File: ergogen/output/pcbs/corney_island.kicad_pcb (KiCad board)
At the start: 2 copper layers, 133.8 x 91.7 mm, 101 parts

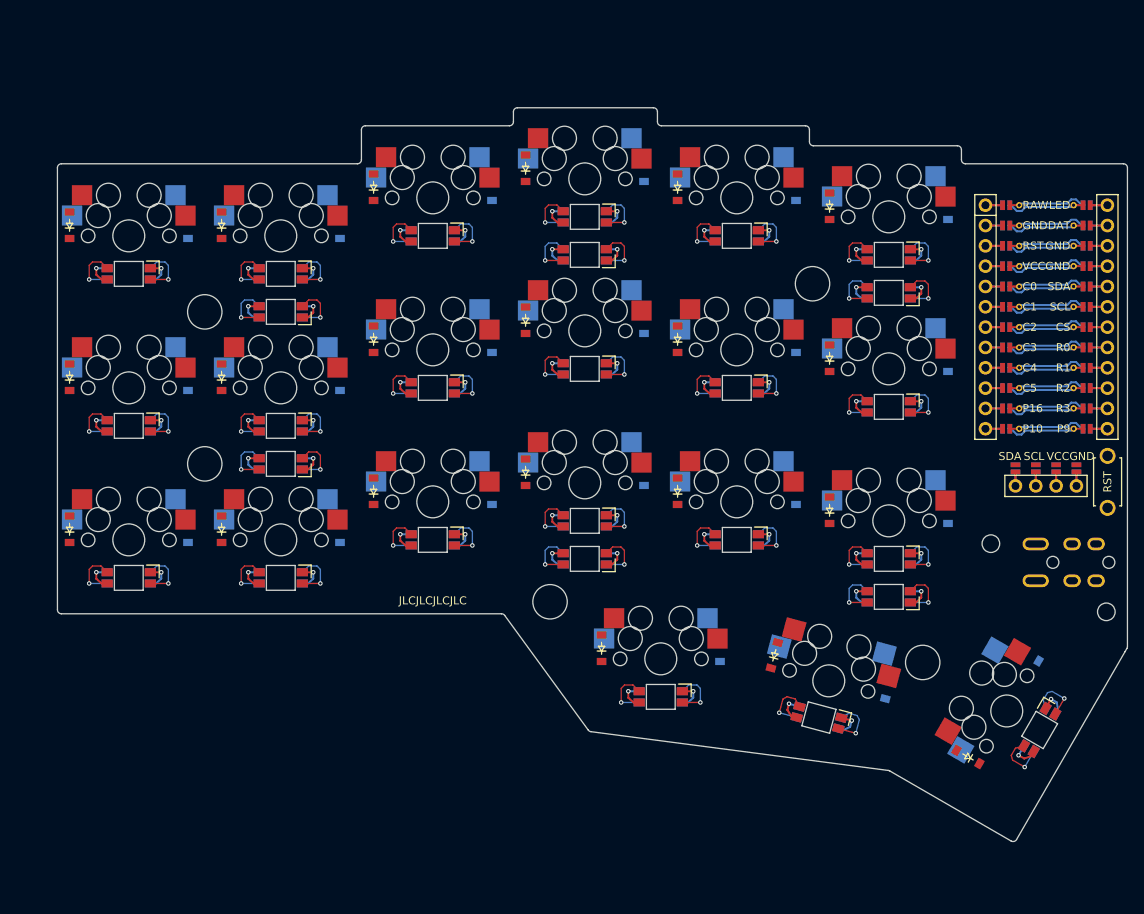
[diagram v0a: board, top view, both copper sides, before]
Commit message: Removed outer column
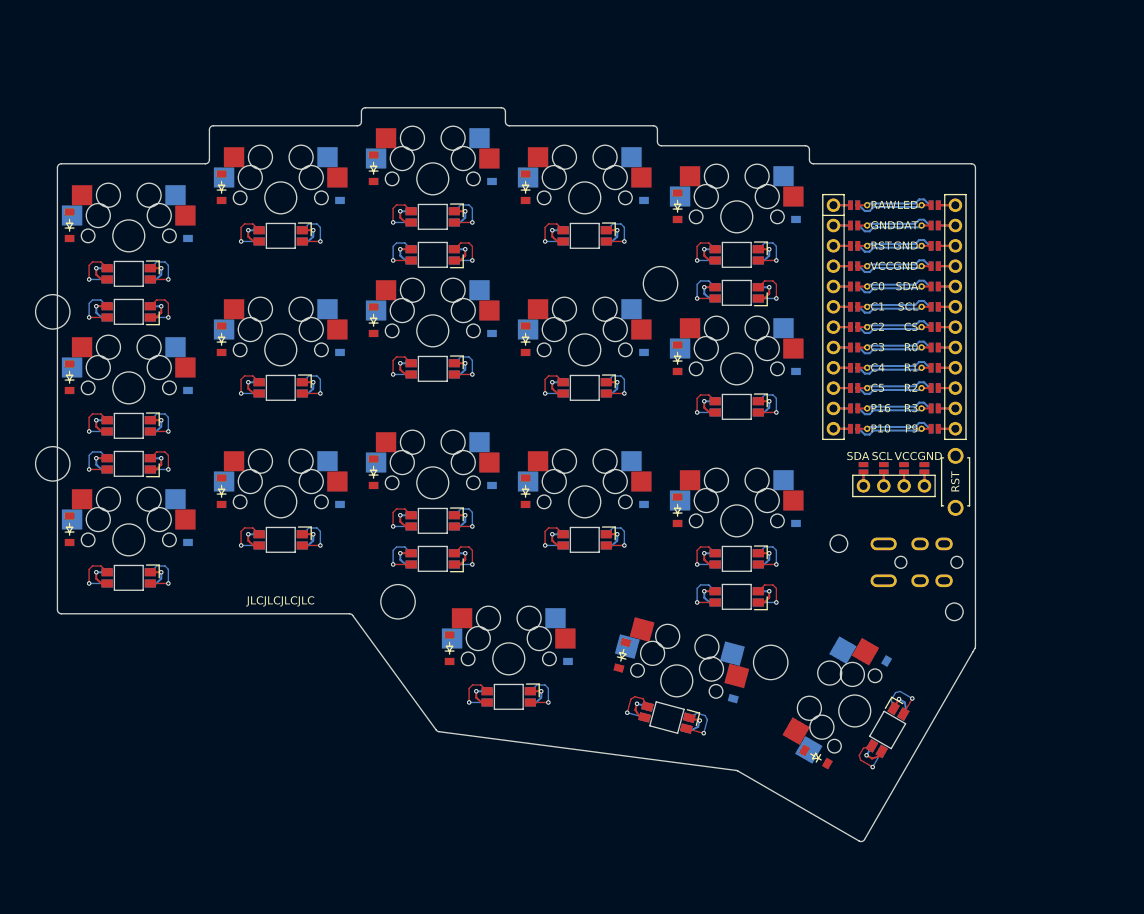
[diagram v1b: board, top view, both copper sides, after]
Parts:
- removed D37, D38, D39, D40, D41, D42: , ceoloide:diode_tht_sod123
- removed LED25, LED26, LED27: , ceoloide:led_SK6812mini-e (underglow, reversible)
- removed S19, S20, S21: , MX
- D19, D20, D21: moved to F.Cu
- LED19, LED20, LED21: footprint ceoloide:led_SK6812mini-e (per-key, reversible) -> ceoloide:led_SK6812mini-e (underglow, reversible)
- moved D21 131.2 mm to (92.6, 60.7), turned to 90 degrees
- moved LED21 125.3 mm to (100.0, 71.5), turned to 180 degrees
- moved D20 109.4 mm to (92.6, 79.7), turned to 90 degrees
- moved LED22 97.4 mm to (100.0, 90.5)
- moved D19 82.6 mm to (92.6, 98.7)
- moved LED20 75.3 mm to (138.0, 64.4), turned to 180 degrees
- moved D36 73.3 mm to (185.9, 127.1), turned to 150 degrees
- moved LED24 67.2 mm to (176.0, 107.1)
- moved S18 61.9 mm to (190.7, 121.4), turned to 60 degrees
- moved LED18 59.4 mm to (194.9, 123.8), turned to 240 degrees
- moved D18 56.8 mm to (193.3, 114.3), turned to 150 degrees
- moved LED19 51.4 mm to (176.0, 69.1)
- moved D16 50.5 mm to (154.9, 113.5)
- moved LED16 50.5 mm to (147.5, 119.6)
- moved S16 50.5 mm to (147.5, 114.9)
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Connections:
- D1 pad 2: outer_bottom -> pinky_bottom
- D10 pad 2: middle_bottom -> index_bottom
- D11 pad 2: middle_home -> index_home
- D12 pad 2: middle_top -> index_top
- D13 pad 2: index_bottom -> inner_bottom
- D14 pad 2: index_home -> inner_home
- D15 pad 2: index_top -> inner_top
- D16 pad 1: R2 -> R3
- D16 pad 2: inner_bottom -> near_home
- D17 pad 1: R1 -> R3
- D17 pad 2: inner_home -> mid_home
- D18 pad 1: R0 -> R3
- D18 pad 2: inner_top -> far_home
- D19 pad 1: R3 -> R2
- D19 pad 2: near_home -> pinky_bottom
- D2 pad 2: outer_home -> pinky_home
- D20 pad 1: R3 -> R1
- D20 pad 2: mid_home -> pinky_home
- D21 pad 1: R3 -> R0
- D21 pad 2: far_home -> pinky_top
- D22 pad 2: outer_bottom -> ring_bottom
- D23 pad 2: outer_home -> ring_home
- D24 pad 2: outer_top -> ring_top
- D25 pad 2: pinky_bottom -> middle_bottom
- D26 pad 2: pinky_home -> middle_home
- D27 pad 2: pinky_top -> middle_top
- D28 pad 2: ring_bottom -> index_bottom
- D29 pad 2: ring_home -> index_home
- D3 pad 2: outer_top -> pinky_top
- D30 pad 2: ring_top -> index_top
- D31 pad 2: middle_bottom -> inner_bottom
- D32 pad 2: middle_home -> inner_home
- D33 pad 2: middle_top -> inner_top
- D34 pad 1: R2 -> R3
- D34 pad 2: index_bottom -> near_home
- D35 pad 1: R1 -> R3
- D35 pad 2: index_home -> mid_home
- D36 pad 1: R0 -> R3
- D36 pad 2: index_top -> far_home
- D4 pad 2: pinky_bottom -> ring_bottom
- D5 pad 2: pinky_home -> ring_home
- D6 pad 2: pinky_top -> ring_top
- D7 pad 2: ring_bottom -> middle_bottom
- D8 pad 2: ring_home -> middle_home
- D9 pad 2: ring_top -> middle_top
- LED1 pad 2: LED_21 -> LED_16
- LED1 pad 4: LED_20 -> LED_15
- LED10 pad 2: LED_10 -> LED_7
- LED10 pad 4: LED_9 -> LED_6
- LED11 pad 2: LED_11 -> LED_6
- LED11 pad 4: LED_10 -> LED_5
- LED12 pad 2: LED_12 -> LED_5
- LED12 pad 4: LED_11 -> LED_4
- LED13 pad 2: LED_7 -> LED_2
- LED13 pad 4: LED_6 -> LED_1
- LED14 pad 2: LED_6 -> LED_3
- LED14 pad 4: LED_5 -> LED_2
- LED15 pad 2: LED_5 -> LED_4
- LED15 pad 4: LED_4 -> LED_3
- LED16 pad 2: LED_2 -> LED_9
- LED16 pad 4: LED_1 -> LED_8
- LED17 pad 2: LED_3 -> LED_8
- LED17 pad 4: LED_2 -> LED_7
- LED18 pad 2: LED_4 -> LED_1
- LED18 pad 4: LED_3 -> ULED_6
- LED19 pad 2: LED_9 -> ULED_1
- LED19 pad 4: LED_8 -> LED
- LED2 pad 2: LED_20 -> LED_17
- LED2 pad 4: LED_19 -> LED_16
- LED20 pad 2: LED_8 -> ULED_2
- LED20 pad 4: LED_7 -> ULED_1
- LED21 pad 2: LED_1 -> ULED_3
- LED21 pad 4: ULED_6 -> ULED_2
- LED22 pad 2: ULED_1 -> ULED_4
- LED22 pad 4: LED -> ULED_3
- LED23 pad 2: ULED_2 -> ULED_5
- LED23 pad 4: ULED_1 -> ULED_4
- LED24 pad 2: ULED_3 -> ULED_6
- LED24 pad 4: ULED_2 -> ULED_5
- LED3 pad 2: LED_19 -> LED_18
- LED3 pad 4: LED_18 -> LED_17
- LED4 pad 2: LED_16 -> LED_15
- LED4 pad 4: LED_15 -> LED_14
- LED5 pad 2: LED_17 -> LED_14
- LED5 pad 4: LED_16 -> LED_13
- LED6 pad 2: LED_18 -> LED_13
- LED6 pad 4: LED_17 -> LED_12
- LED7 pad 2: LED_15 -> LED_10
- LED7 pad 4: LED_14 -> LED_9
- LED8 pad 2: LED_14 -> LED_11
- LED8 pad 4: LED_13 -> LED_10
- LED9 pad 2: LED_13 -> LED_12
- LED9 pad 4: LED_12 -> LED_11
- MCU1 pad 1: MCU1_1 -> LED
- MCU1 pad 10: MCU1_10 -> R2
- MCU1 pad 11: MCU1_11 -> R3
- MCU1 pad 12: MCU1_12 -> P9
- MCU1 pad 2: MCU1_2 -> DAT
- MCU1 pad 3: MCU1_3 -> GND
- MCU1 pad 4: MCU1_4 -> GND
- MCU1 pad 5: MCU1_5 -> SDA
- MCU1 pad 6: MCU1_6 -> SCL
- MCU1 pad 7: MCU1_7 -> CS
- MCU1 pad 8: MCU1_8 -> R0
- MCU1 pad 9: MCU1_9 -> R1
- S1 pad 1: C0 -> C1
- S1 pad 2: outer_bottom -> pinky_bottom
- S10 pad 1: C3 -> C4
- S10 pad 2: middle_bottom -> index_bottom
- S11 pad 1: C3 -> C4
- S11 pad 2: middle_home -> index_home
- S12 pad 1: C3 -> C4
- S12 pad 2: middle_top -> index_top
- S13 pad 1: C4 -> C5
- S13 pad 2: index_bottom -> inner_bottom
- S14 pad 1: C4 -> C5
- S14 pad 2: index_home -> inner_home
- S15 pad 1: C4 -> C5
- S15 pad 2: index_top -> inner_top
- S16 pad 1: C5 -> C3
- S16 pad 2: inner_bottom -> near_home
- S17 pad 1: C5 -> C4
- S17 pad 2: inner_home -> mid_home
- S18 pad 2: inner_top -> far_home
- S2 pad 1: C0 -> C1
- S2 pad 2: outer_home -> pinky_home
- S3 pad 1: C0 -> C1
- S3 pad 2: outer_top -> pinky_top
- S4 pad 1: C1 -> C2
- S4 pad 2: pinky_bottom -> ring_bottom
- S5 pad 1: C1 -> C2
- S5 pad 2: pinky_home -> ring_home
- S6 pad 1: C1 -> C2
- S6 pad 2: pinky_top -> ring_top
- S7 pad 1: C2 -> C3
- S7 pad 2: ring_bottom -> middle_bottom
- S8 pad 1: C2 -> C3
- S8 pad 2: ring_home -> middle_home
- S9 pad 1: C2 -> C3
- S9 pad 2: ring_top -> middle_top
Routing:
- net inner_top: track 0.00 -> 101.6 mm
- net pinky_bottom: track 0.00 -> 101.4 mm
- net far_home: track 0.00 -> 50.9 mm
- net R2: track 9.63 -> 50.9 mm
- net GND: track 130.3 -> 93.6 mm, vias 27 -> 24
- net VCC: track 111.0 -> 93.6 mm, vias 27 -> 24
- net LED_20: track 13.5 -> 0.00 mm, vias 2 -> 0
- net LED_19: track 13.5 -> 0.00 mm, vias 2 -> 0
- net C3: track 9.64 -> 0.00 mm
- net RST: track 9.64 -> 0.00 mm
- net RAW: track 9.64 -> 0.00 mm
- net P16: track 9.64 -> 0.00 mm
- net C2: track 9.64 -> 0.00 mm
- net C0: track 9.64 -> 0.00 mm
- net P10: track 9.64 -> 0.00 mm
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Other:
- board size 133.8 x 91.7 mm -> 114.8 x 91.7 mm

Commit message: Changed stagger to be like karia
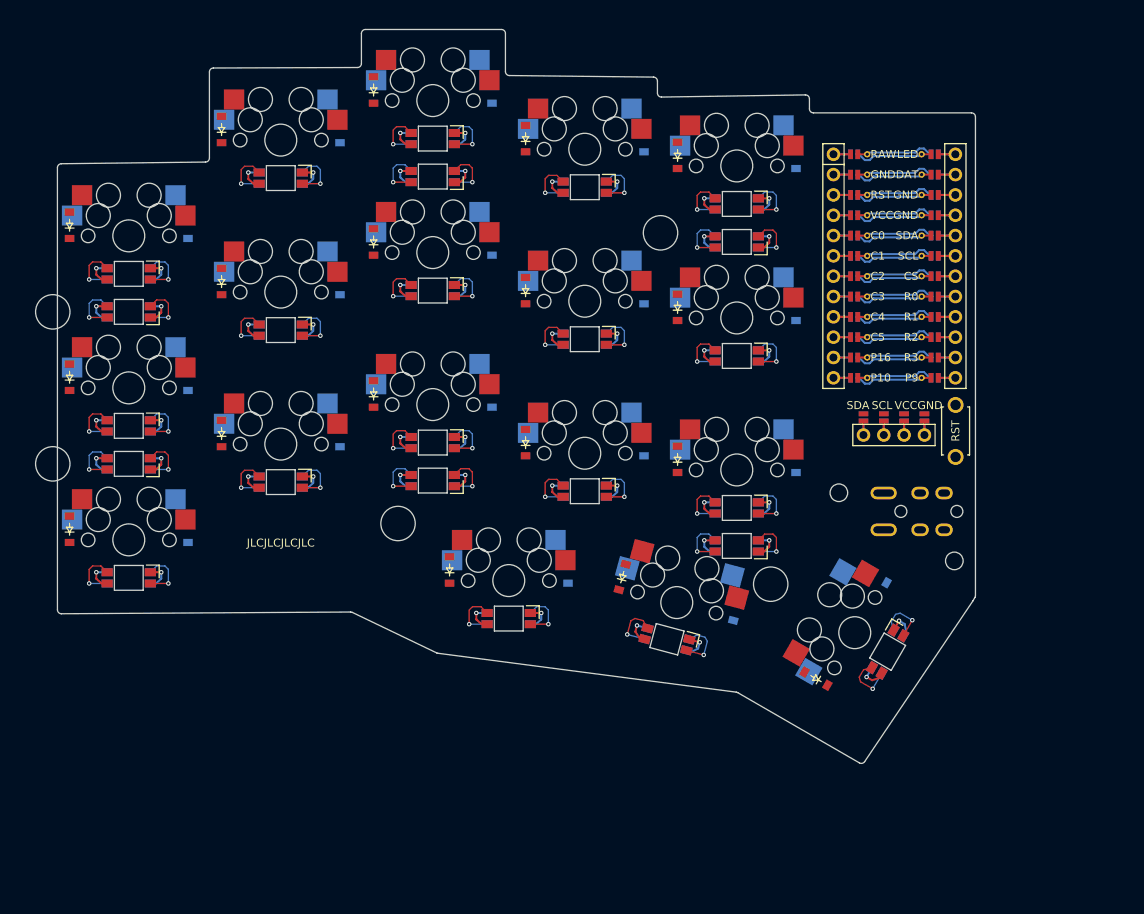
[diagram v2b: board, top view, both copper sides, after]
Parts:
- moved D16 9.78 mm to (154.9, 103.8)
- moved D17 9.78 mm to (176.0, 108.5)
- moved D18 9.78 mm to (193.3, 104.5)
- moved D25 9.78 mm to (130.6, 81.8)
- moved D26 9.78 mm to (130.6, 62.8)
- moved D27 9.78 mm to (130.6, 43.8)
- moved D34 9.78 mm to (140.1, 103.8)
- moved D35 9.78 mm to (161.7, 104.6)
- moved D36 9.78 mm to (185.9, 117.4)
- moved D7 9.78 mm to (145.4, 81.8)
- moved D8 9.78 mm to (145.4, 62.8)
- moved D9 9.78 mm to (145.4, 43.8)
- moved LED16 9.78 mm to (147.5, 109.8)
- moved LED17 9.78 mm to (167.3, 112.4)
- moved LED18 9.78 mm to (194.9, 114.0)
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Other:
- outline, holes or cut-outs redrawn

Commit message: Added splay to pinky
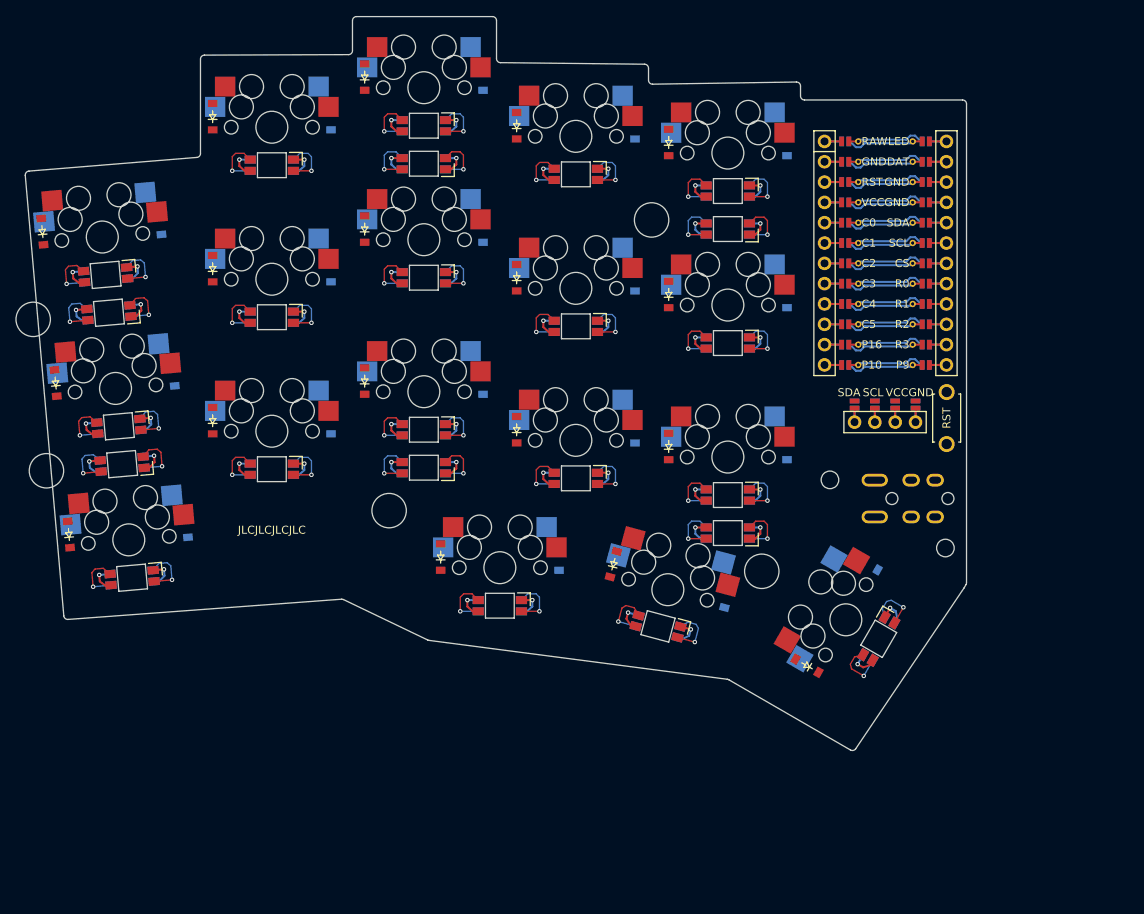
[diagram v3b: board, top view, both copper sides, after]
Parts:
- moved D3 3.49 mm to (103.9, 60.2), turned to 95 degrees
- moved D21 3.49 mm to (89.2, 61.5), turned to 95 degrees
- moved S3 3.32 mm to (96.7, 62.1), turned to 5 degrees
- moved LED3 2.90 mm to (97.1, 66.9), turned to 185 degrees
- moved MH3 2.62 mm to (88.1, 72.4), turned to 5 degrees
- moved LED21 2.49 mm to (97.5, 71.6), turned to 185 degrees
- moved LED17 1.96 mm to (166.2, 110.8)
- moved D16 1.96 mm to (153.8, 102.2)
- moved D17 1.96 mm to (174.9, 106.9)
- moved D18 1.96 mm to (192.2, 102.9)
- moved D25 1.96 mm to (129.5, 80.2)
- moved D26 1.96 mm to (129.5, 61.2)
- moved D27 1.96 mm to (129.5, 42.2)
- moved D34 1.96 mm to (139.0, 102.2)
- moved D35 1.96 mm to (160.6, 103.0)
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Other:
- board size 114.8 x 91.7 mm -> 117.7 x 91.7 mm

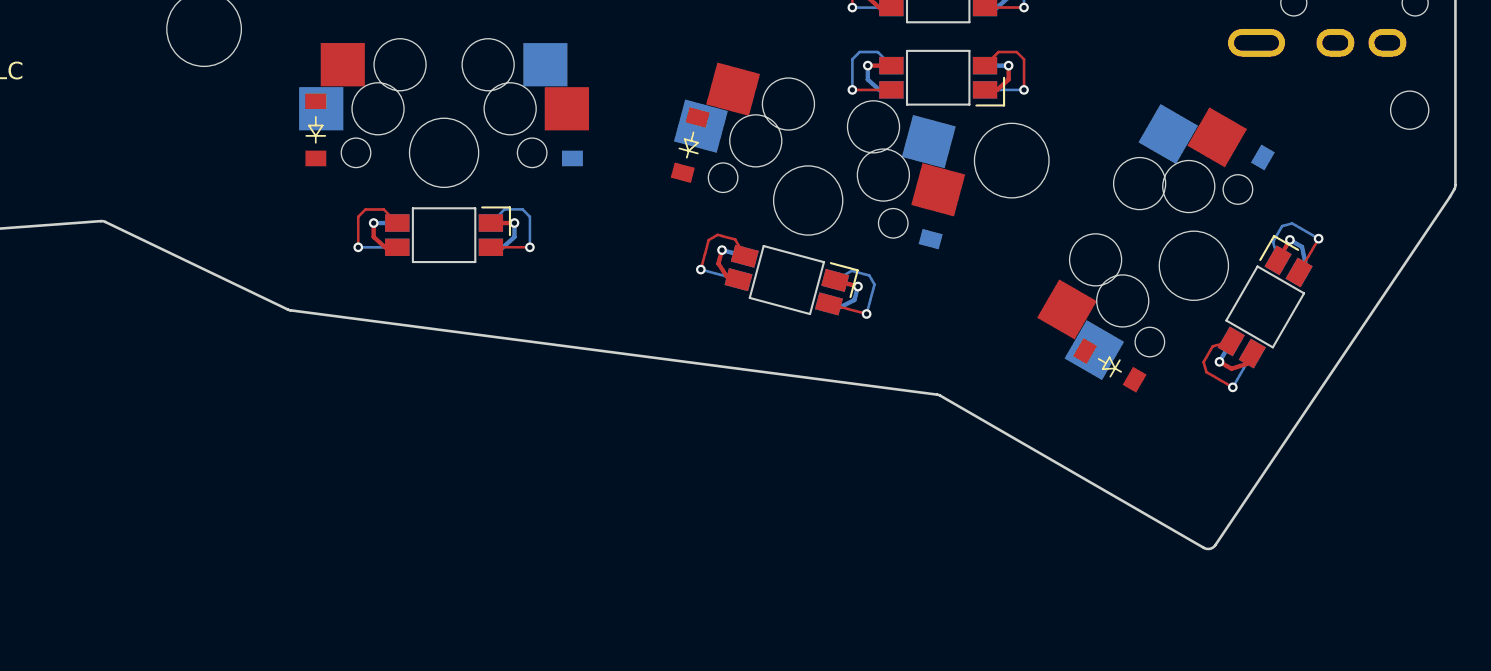
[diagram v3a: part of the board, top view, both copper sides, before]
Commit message: Changed thumb key back to 1u
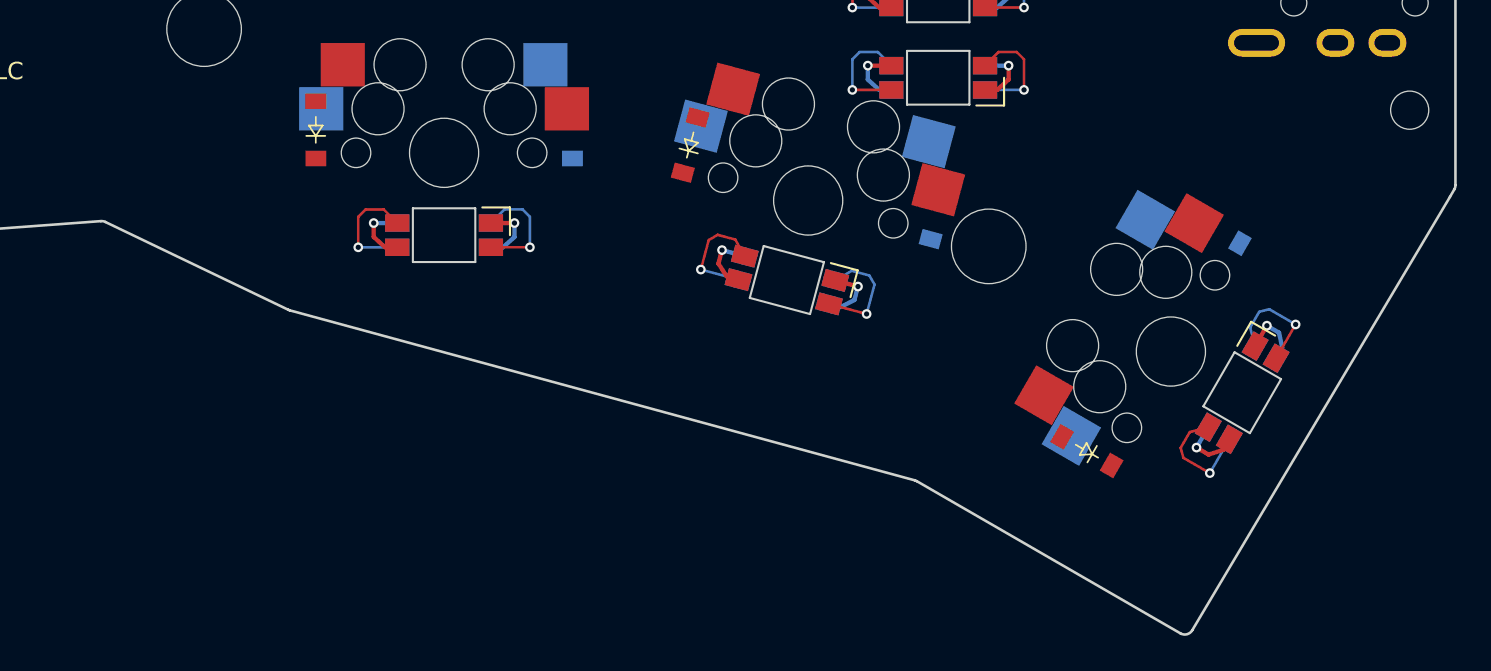
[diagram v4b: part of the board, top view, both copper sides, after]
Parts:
- moved D18 5.12 mm to (190.9, 107.9)
- moved D36 5.12 mm to (183.5, 120.7)
- moved LED18 5.12 mm to (192.4, 117.3)
- moved MH7 5.12 mm to (177.8, 108.9)
- moved S18 5.12 mm to (188.3, 114.9)
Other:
- board size 117.7 x 91.7 mm -> 117.7 x 96.7 mm
